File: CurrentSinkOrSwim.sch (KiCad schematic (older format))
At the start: 0 parts

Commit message: Adding preliminary components (without values) to the schematic.
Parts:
- added C? (x2): C, symbol C
- added P?: CONN_01X02, symbol CONN_01X02
- added Q?: MOSFET_N, symbol MOSFET_N
- added R? (x2): R, symbol R
- added RV?: POT, symbol POT
- added U? (x2): LMV358, symbol LMV358
- added U?: TC1016, symbol TC1016
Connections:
- net labels added: GND
- wire segments 0 -> 36

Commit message: Updating The Schematic With Part Numbers
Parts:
- removed U?: TC1016, symbol TC1016
- added C?: C, symbol C
- added R?: 0, symbol R
- added U?: TC1016, symbol TC1016
- Q?: value MOSFET_N -> BUK9575; MPN (none) -> BUK9575-100A,127
- R?: value R -> .1; MPN (none) -> AC01000001007JA100
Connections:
- net labels added: 2.7V
- wire segments 36 -> 34
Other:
- moved on the sheet: C?, P?
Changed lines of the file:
@@
 P 6950 4550
 F 0 "R?" V 7030 4550 50  0000 C CNN
-F 1 "R" V 6957 4551 50  0000 C CNN
+F 1 ".1" V 6957 4551 50  0000 C CNN
 F 2 "" V 6880 4550 30  0000 C CNN
 F 3 "" H 6950 4550 30  0000 C CNN
+F 4 "AC01000001007JA100" V 6950 4550 60  0001 C CNN "MPN"
 	1    6950 4550
 	1    0    0    -1
@@
 P 6850 3100
 F 0 "Q?" H 6860 3270 50  0000 R CNN
-F 1 "MOSFET_N" H 6800 2950 50  0000 R CNN
+F 1 "BUK9575" H 6800 2950 50  0000 R CNN
 F 2 "" H 6850 3100 60  0000 C CNN
 F 3 "" H 6850 3100 60  0000 C CNN
+F 4 "BUK9575-100A,127" H 6850 3100 60  0001 C CNN "MPN"
 	1    6850 3100
 	1    0    0    -1
@@
 $EndComp
 Wire Wire Line
-	6950 4800 6950 4850
-Wire Wire Line
-	6950 4850 6950 5000
-Wire Wire Line
-	6950 3300 6950 4000
-Wire Wire Line
-	6950 4000 6950 4300
+	6950 4800 6950 5000
+Wire Wire Line
+	6950 3300 6950 4300
 Wire Wire Line
 	6650 3100 6000 3100
@@
 Connection ~ 6950 4000
 Wire Wire Line
-	5400 1950 5400 2700
-Wire Wire Line
 	5000 3000 4150 3000
 Wire Wire Line
@@
 	4150 3950 3600 3950
 Wire Wire Line
-	3600 3850 3600 3950
-Wire Wire Line
-	3600 3950 3600 4050
+	3600 3850 3600 4050
 Connection ~ 3600 3950
 Wire Wire Line
@@
 Connection ~ 6950 4850
 Wire Wire Line
-	6500 1950 6600 1950
-Wire Wire Line
-	6600 1950 6950 1950
-Wire Wire Line
-	6950 1950 8100 1950
-Wire Wire Line
-	6950 1950 6950 2900
-$Comp
-L TC1016 U?
-U 1 1 54CE8C07
-P 6100 2000
-F 0 "U?" H 6250 1804 60  0000 C CNN
-F 1 "TC1016" H 6100 2200 60  0000 C CNN
-F 2 "" H 6100 2000 60  0000 C CNN
-F 3 "" H 6100 2000 60  0000 C CNN
-	1    6100 2000
-	-1   0    0    -1
-$EndComp
-Connection ~ 6950 1950
-Connection ~ 5400 1950
+	6200 1250 8100 1250
+Wire Wire Line
+	6950 1250 6950 2900
+Connection ~ 6950 1250
 $Comp
 L GND #PWR?
 U 1 1 54CE8D06
-P 6100 2500
-F 0 "#PWR?" H 6100 2250 60  0001 C CNN
-F 1 "GND" H 6100 2350 60  0000 C CNN
-F 2 "" H 6100 2500 60  0000 C CNN
-F 3 "" H 6100 2500 60  0000 C CNN
-	1    6100 2500
-	1    0    0    -1
-$EndComp
-Wire Wire Line
-	6100 2500 6100 2450
-Wire Wire Line
-	6100 2450 6100 2350
-Wire Wire Line
-	6100 2350 6100 2250
+P 5800 2150
+F 0 "#PWR?" H 5800 1900 60  0001 C CNN
+F 1 "GND" H 5800 2000 60  0000 C CNN
+F 2 "" H 5800 2150 60  0000 C CNN
+F 3 "" H 5800 2150 60  0000 C CNN
+	1    5800 2150
+	1    0    0    -1
+$EndComp
 $Comp
 L C C?
 U 1 1 54CE8F07
-P 6600 2250
-F 0 "C?" H 6650 2350 50  0000 L CNN
-F 1 "C" H 6650 2150 50  0000 L CNN
-F 2 "" H 6638 2100 30  0000 C CNN
-F 3 "" H 6600 2250 60  0000 C CNN
-	1    6600 2250
+P 6600 1550
+F 0 "C?" H 6650 1650 50  0000 L CNN
+F 1 "C" H 6650 1450 50  0000 L CNN
+F 2 "" H 6638 1400 30  0000 C CNN
+F 3 "" H 6600 1550 60  0000 C CNN
+	1    6600 1550
 	1    0    0    -1
 $EndComp
@@
 L C C?
 U 1 1 54CE8F9A
-P 5600 2250
-F 0 "C?" H 5650 2350 50  0000 L CNN
-F 1 "C" H 5650 2150 50  0000 L CNN
-F 2 "" H 5638 2100 30  0000 C CNN
-F 3 "" H 5600 2250 60  0000 C CNN
-	1    5600 2250
-	1    0    0    -1
-$EndComp
-Wire Wire Line
-	5600 1950 5600 2050
-Connection ~ 5600 1950
-Wire Wire Line
-	5600 2450 6100 2450
-Connection ~ 6100 2450
-Wire Wire Line
-	6600 2450 6250 2450
-Wire Wire Line
-	6250 2450 6250 2350
-Wire Wire Line
-	6250 2350 6100 2350
-Connection ~ 6100 2350
-Wire Wire Line
-	6600 2050 6600 1950
-Connection ~ 6600 1950
+P 5000 1600
+F 0 "C?" H 5050 1700 50  0000 L CNN
+F 1 "C" H 5050 1500 50  0000 L CNN
+F 2 "" H 5038 1450 30  0000 C CNN
+F 3 "" H 5000 1600 60  0000 C CNN
+	1    5000 1600
+	1    0    0    -1
+$EndComp
+Wire Wire Line
+	6600 1350 6600 1250
+Connection ~ 6600 1250
 $Comp
 L POT RV?
@@
 $EndComp
 Wire Wire Line
-	3750 3600 3750 1950
-Wire Wire Line
-	3750 1950 5400 1950
-Wire Wire Line
-	5400 1950 5600 1950
-Wire Wire Line
-	5600 1950 5700 1950
+	3750 1250 3750 3600
 $Comp
 L CONN_01X02 P?
 U 1 1 54CEA02B
-P 8300 2000
-F 0 "P?" H 8300 2150 50  0000 C CNN
-F 1 "CONN_01X02" V 8400 2000 50  0000 C CNN
-F 2 "" H 8300 2000 60  0000 C CNN
-F 3 "" H 8300 2000 60  0000 C CNN
-	1    8300 2000
-	1    0    0    -1
-$EndComp
-Wire Wire Line
-	8100 2050 7900 2050
-Wire Wire Line
-	7900 2050 7900 2350
+P 8300 1300
+F 0 "P?" H 8300 1450 50  0000 C CNN
+F 1 "CONN_01X02" V 8400 1300 50  0000 C CNN
+F 2 "" H 8300 1300 60  0000 C CNN
+F 3 "" H 8300 1300 60  0000 C CNN
+	1    8300 1300
+	1    0    0    -1
+$EndComp
+Wire Wire Line
+	8100 1350 7900 1350
+Wire Wire Line
+	7900 1350 7900 2350
 $Comp
 L GND #PWR?
@@
 	1    0    0    -1
 $EndComp
+$Comp
+L TC1016 U?
+U 1 1 54D813FD
+P 5800 1450
+F 0 "U?" H 5950 1254 60  0000 C CNN
+F 1 "TC1016" H 5800 1850 60  0000 C CNN
+F 2 "" H 5800 1450 60  0000 C CNN
+F 3 "" H 5800 1450 60  0000 C CNN
+	1    5800 1450
+	-1   0    0    -1
+$EndComp
+Wire Wire Line
+	6600 1750 6600 2050
+Wire Wire Line
+	3750 1250 5400 1250
+Wire Wire Line
+	5000 1250 5000 1400
+Wire Wire Line
+	5000 1800 5000 1900
+Wire Wire Line
+	5000 1900 5800 1900
+Connection ~ 6400 1250
+$Comp
+L R R?
+U 1 1 54D81C67
+P 6400 1550
+F 0 "R?" V 6480 1550 40  0000 C CNN
+F 1 "0" V 6407 1551 40  0000 C CNN
+F 2 "" V 6330 1550 30  0000 C CNN
+F 3 "" H 6400 1550 30  0000 C CNN
+F 4 "Value" H 6400 1550 60  0001 C CNN "MPN"
+	1    6400 1550
+	1    0    0    -1
+$EndComp
+Wire Wire Line
+	5800 1700 5800 2150
+Wire Wire Line
+	6600 2050 5800 2050
+Connection ~ 5800 2050
+Wire Wire Line
+	6400 1300 6400 1250
+Wire Wire Line
+	6400 1800 6400 1900
+Wire Wire Line
+	6400 1900 6200 1900
+Wire Wire Line
+	6200 1900 6200 1400
+Connection ~ 5000 1250
+Wire Wire Line
+	3750 2250 5400 2250
+Wire Wire Line
+	5400 2250 5400 2700
+Connection ~ 3750 2250
+$Comp
+L GND #PWR?
+U 1 1 54D82007
+P 4800 2800
+F 0 "#PWR?" H 4800 2550 60  0001 C CNN
+F 1 "GND" H 4800 2650 60  0000 C CNN
+F 2 "" H 4800 2800 60  0000 C CNN
+F 3 "" H 4800 2800 60  0000 C CNN
+	1    4800 2800
+	1    0    0    -1
+$EndComp
+$Comp
+L C C?
+U 1 1 54D8201D
+P 4800 2550
+F 0 "C?" H 4850 2650 50  0000 L CNN
+F 1 "C" H 4850 2450 50  0000 L CNN
+F 2 "" H 4838 2400 30  0000 C CNN
+F 3 "" H 4800 2550 60  0000 C CNN
+	1    4800 2550
+	1    0    0    -1
+$EndComp
+Wire Wire Line
+	4800 2350 4800 2250
+Connection ~ 4800 2250
+Wire Wire Line
+	4800 2800 4800 2750
+Text Label 4400 2250 0    60   ~ 0
+2.7V
 $EndSCHEMATC

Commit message: Finding A Higher Rated Linear Regulator
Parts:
- removed U?: TC1016, symbol TC1016
- added P?: CONN_01X03, symbol CONN_01X03
- added P?: CONN_01X02, symbol CONN_01X02
- added R?: 27K, symbol R
- added R?: 21.6K, symbol R
- added U?: LM2931D-R, symbol LM2931D-R
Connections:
- wire segments 34 -> 52
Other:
- note added: "Battery Pack"
- note added: "Current Sink Input"
- moved on the sheet: C?, R?
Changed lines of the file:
@@
 	3600 4850 6950 4850
 Connection ~ 6950 4850
-Wire Wire Line
-	6200 1250 8100 1250
-Wire Wire Line
-	6950 1250 6950 2900
-Connection ~ 6950 1250
 $Comp
 L GND #PWR?
@@
 L C C?
 U 1 1 54CE8F9A
-P 5000 1600
-F 0 "C?" H 5050 1700 50  0000 L CNN
-F 1 "C" H 5050 1500 50  0000 L CNN
-F 2 "" H 5038 1450 30  0000 C CNN
-F 3 "" H 5000 1600 60  0000 C CNN
-	1    5000 1600
-	1    0    0    -1
-$EndComp
-Wire Wire Line
-	6600 1350 6600 1250
-Connection ~ 6600 1250
+P 4400 1700
+F 0 "C?" H 4450 1800 50  0000 L CNN
+F 1 "C" H 4450 1600 50  0000 L CNN
+F 2 "" H 4438 1550 30  0000 C CNN
+F 3 "" H 4400 1700 60  0000 C CNN
+	1    4400 1700
+	1    0    0    -1
+$EndComp
 $Comp
 L POT RV?
@@
 $EndComp
 Wire Wire Line
-	3750 1250 3750 3600
+	3750 900  3750 3600
 $Comp
 L CONN_01X02 P?
@@
 	1    0    0    -1
 $EndComp
-$Comp
-L TC1016 U?
-U 1 1 54D813FD
-P 5800 1450
-F 0 "U?" H 5950 1254 60  0000 C CNN
-F 1 "TC1016" H 5800 1850 60  0000 C CNN
-F 2 "" H 5800 1450 60  0000 C CNN
-F 3 "" H 5800 1450 60  0000 C CNN
-	1    5800 1450
-	-1   0    0    -1
-$EndComp
-Wire Wire Line
-	6600 1750 6600 2050
-Wire Wire Line
-	3750 1250 5400 1250
-Wire Wire Line
-	5000 1250 5000 1400
-Wire Wire Line
-	5000 1800 5000 1900
-Wire Wire Line
-	5000 1900 5800 1900
-Connection ~ 6400 1250
+Wire Wire Line
+	6600 2050 6600 1750
 $Comp
 L R R?
 U 1 1 54D81C67
-P 6400 1550
-F 0 "R?" V 6480 1550 40  0000 C CNN
-F 1 "0" V 6407 1551 40  0000 C CNN
-F 2 "" V 6330 1550 30  0000 C CNN
-F 3 "" H 6400 1550 30  0000 C CNN
-F 4 "Value" H 6400 1550 60  0001 C CNN "MPN"
-	1    6400 1550
+P 6400 1450
+F 0 "R?" V 6480 1450 40  0000 C CNN
+F 1 "0" V 6407 1451 40  0000 C CNN
+F 2 "" V 6330 1450 30  0000 C CNN
+F 3 "" H 6400 1450 30  0000 C CNN
+F 4 "Value" H 6400 1450 60  0001 C CNN "MPN"
+	1    6400 1450
 	1    0    0    -1
 $EndComp
@@
 	5800 1700 5800 2150
 Wire Wire Line
-	6600 2050 5800 2050
+	5700 2050 6600 2050
 Connection ~ 5800 2050
 Wire Wire Line
-	6400 1300 6400 1250
-Wire Wire Line
-	6400 1800 6400 1900
-Wire Wire Line
-	6400 1900 6200 1900
-Wire Wire Line
-	6200 1900 6200 1400
-Connection ~ 5000 1250
+	6400 1100 6400 1300
 Wire Wire Line
 	3750 2250 5400 2250
@@
 Text Label 4400 2250 0    60   ~ 0
 2.7V
+$Comp
+L LM2931D-R U?
+U 1 1 54D82F07
+P 5850 1400
+F 0 "U?" H 6100 1250 60  0000 C CNN
+F 1 "LM2931D-R" H 5850 2050 60  0000 C CNN
+F 2 "" H 5700 1400 60  0000 C CNN
+F 3 "" H 5700 1400 60  0000 C CNN
+	1    5850 1400
+	-1   0    0    -1
+$EndComp
+Wire Wire Line
+	3750 900  5400 900
+Wire Wire Line
+	4400 900  4400 1500
+Connection ~ 4400 900
+$Comp
+L R R?
+U 1 1 54D8307E
+P 4950 1150
+F 0 "R?" V 5030 1150 40  0000 C CNN
+F 1 "27K" V 4957 1151 40  0000 C CNN
+F 2 "" V 4880 1150 30  0000 C CNN
+F 3 "" H 4950 1150 30  0000 C CNN
+F 4 "Value" H 4950 1150 60  0001 C CNN "MPN"
+	1    4950 1150
+	1    0    0    -1
+$EndComp
+$Comp
+L R R?
+U 1 1 54D83280
+P 4950 1800
+F 0 "R?" V 5030 1800 40  0000 C CNN
+F 1 "21.6K" V 4957 1801 40  0000 C CNN
+F 2 "" V 4880 1800 30  0000 C CNN
+F 3 "" H 4950 1800 30  0000 C CNN
+	1    4950 1800
+	1    0    0    -1
+$EndComp
+Wire Wire Line
+	4400 2100 5800 2100
+Wire Wire Line
+	4950 2100 4950 2050
+Connection ~ 5800 2100
+Wire Wire Line
+	4400 2100 4400 1900
+Connection ~ 4950 2100
+Wire Wire Line
+	4950 1400 4950 1550
+Wire Wire Line
+	5400 1100 5200 1100
+Wire Wire Line
+	5200 1100 5200 1500
+Wire Wire Line
+	5200 1500 4950 1500
+Connection ~ 4950 1500
+Wire Wire Line
+	6300 1100 6400 1100
+Wire Wire Line
+	6600 1350 6600 900
+Wire Wire Line
+	7900 900  7900 1250
+Wire Wire Line
+	7900 1250 8100 1250
+Connection ~ 6600 900
+Wire Wire Line
+	6400 1700 6400 2050
+Connection ~ 6400 2050
+Wire Wire Line
+	5900 1700 5900 2050
+Connection ~ 5900 2050
+Wire Wire Line
+	6000 1700 6000 2050
+Connection ~ 6000 2050
+Wire Wire Line
+	5700 2050 5700 1700
+Wire Wire Line
+	7900 900  6950 900
+Wire Wire Line
+	6950 800  6950 2900
+$Comp
+L CONN_01X03 P?
+U 1 1 54D855F7
+P 6850 600
+F 0 "P?" H 6850 800 50  0000 C CNN
+F 1 "CONN_01X03" V 6950 600 50  0000 C CNN
+F 2 "" H 6850 600 60  0000 C CNN
+F 3 "" H 6850 600 60  0000 C CNN
+	1    6850 600
+	0    -1   -1   0
+$EndComp
+Connection ~ 6950 900
+Wire Wire Line
+	6850 800  6850 900
+Wire Wire Line
+	6850 900  6300 900
+Wire Wire Line
+	6750 800  6350 800
+Wire Wire Line
+	6350 800  6350 650
+Wire Wire Line
+	6350 650  2800 650
+Wire Wire Line
+	2800 650  2800 1250
+$Comp
+L CONN_01X02 P?
+U 1 1 54D858EB
+P 2750 1450
+F 0 "P?" H 2750 1600 50  0000 C CNN
+F 1 "CONN_01X02" V 2850 1450 50  0000 C CNN
+F 2 "" H 2750 1450 60  0000 C CNN
+F 3 "" H 2750 1450 60  0000 C CNN
+	1    2750 1450
+	0    1    1    0
+$EndComp
+$Comp
+L GND #PWR?
+U 1 1 54D85A15
+P 2000 1600
+F 0 "#PWR?" H 2000 1350 60  0001 C CNN
+F 1 "GND" H 2000 1450 60  0000 C CNN
+F 2 "" H 2000 1600 60  0000 C CNN
+F 3 "" H 2000 1600 60  0000 C CNN
+	1    2000 1600
+	1    0    0    -1
+$EndComp
+Wire Wire Line
+	2000 1600 2000 1100
+Wire Wire Line
+	2000 1100 2700 1100
+Wire Wire Line
+	2700 1100 2700 1250
+Text Notes 2500 1750 0    60   ~ 0
+Battery Pack
+Text Notes 8600 1350 0    60   ~ 0
+Current Sink Input
 $EndSCHEMATC

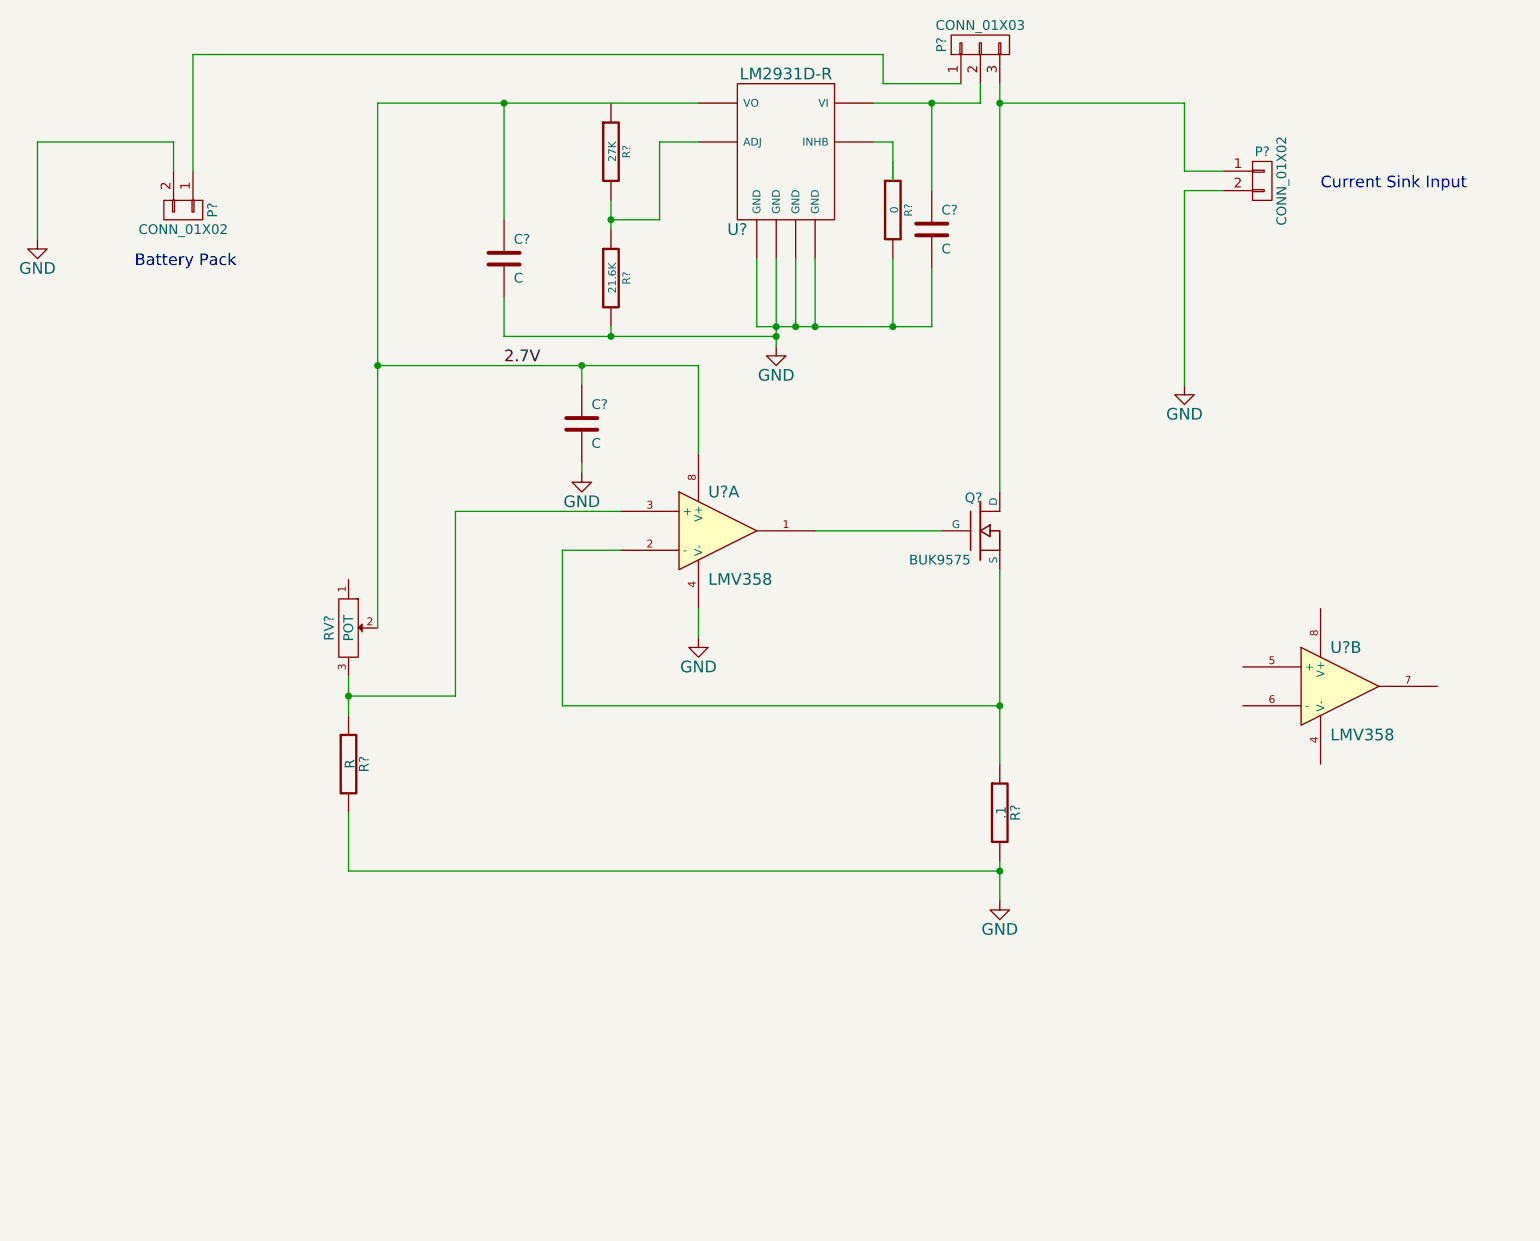
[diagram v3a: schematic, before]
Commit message: Breaking the schematic into hierarchical sheets and updating VoltageControl circuit
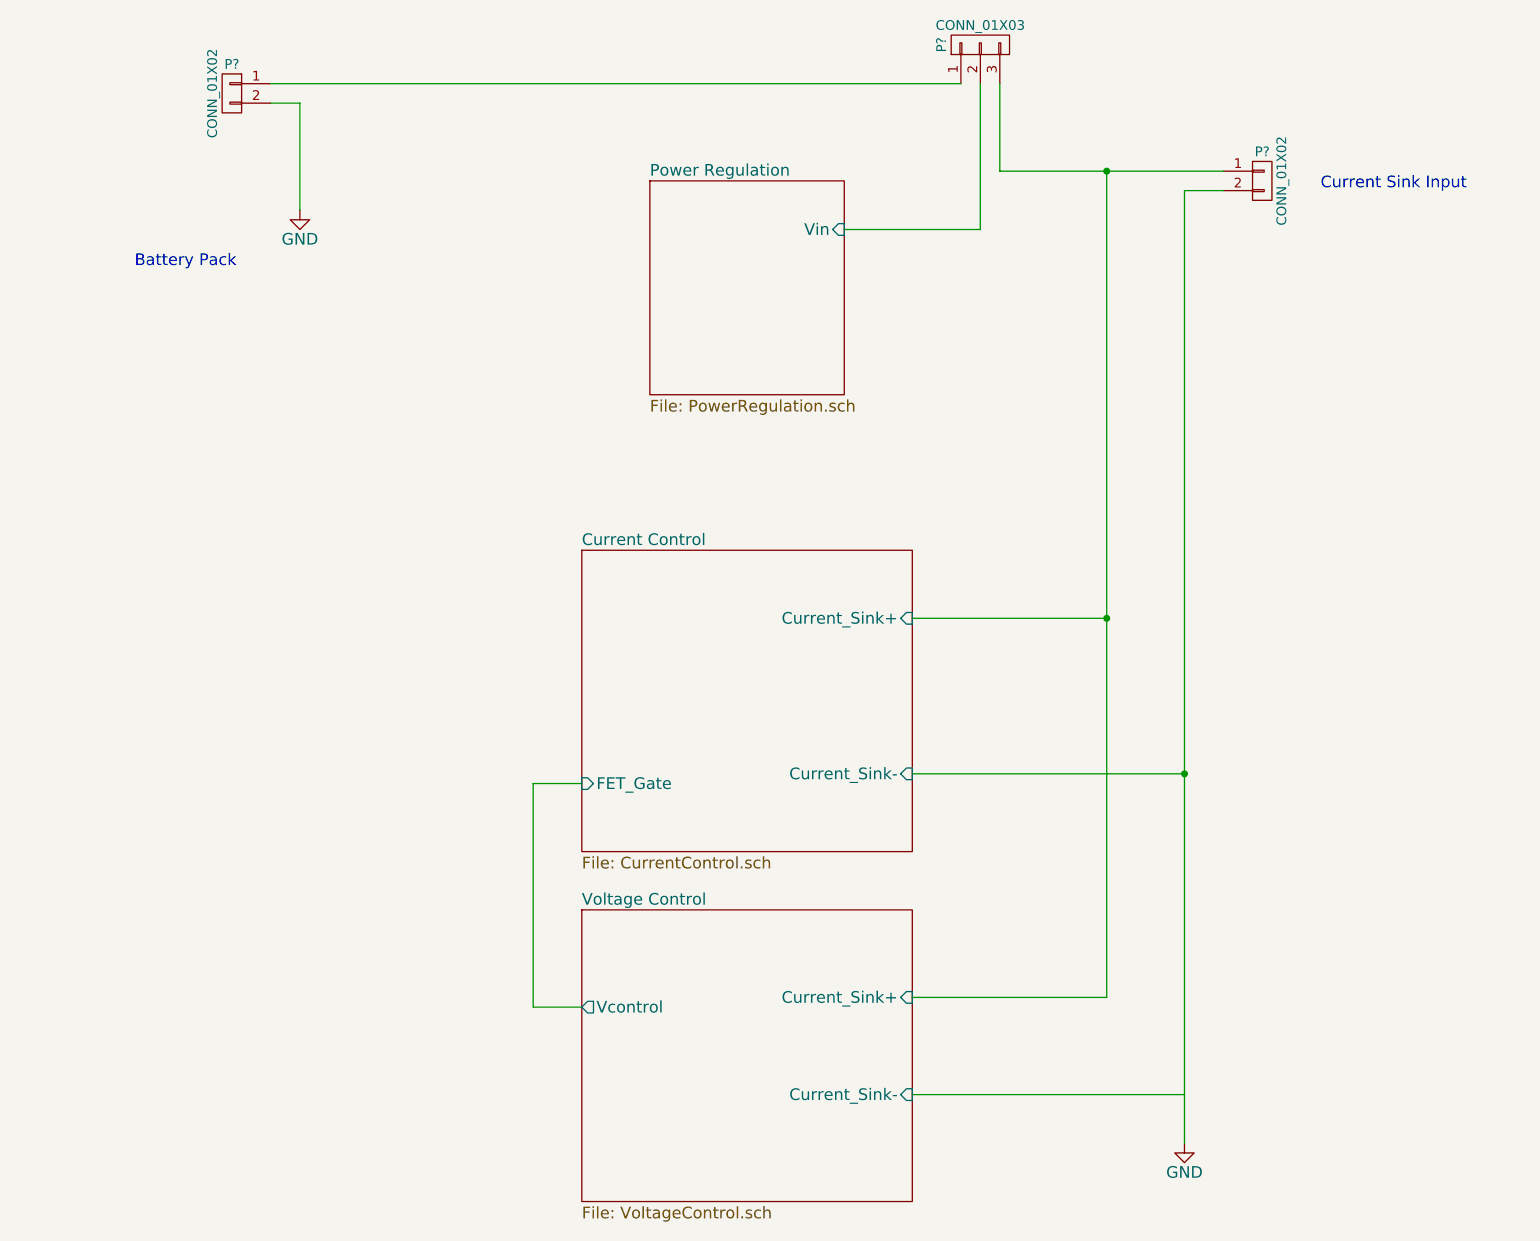
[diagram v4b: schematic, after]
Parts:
- removed C? (x3): C, symbol C
- removed Q?: BUK9575, symbol MOSFET_N
- removed R?: .1, symbol R
- removed R?: R, symbol R
- removed R?: 0, symbol R
- removed R?: 27K, symbol R
- removed R?: 21.6K, symbol R
- removed RV?: POT, symbol POT
- removed U? (x2): LMV358, symbol LMV358
- removed U?: LM2931D-R, symbol LM2931D-R
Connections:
- net labels removed: 2.7V
- wire segments 52 -> 22
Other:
- moved on the sheet: P?

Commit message: Initial Annotation
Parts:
- gave numbers to parts that had none: 3
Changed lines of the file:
@@
 $EndDescr
 $Comp
-L CONN_01X02 P?
+L CONN_01X02 P103
 U 1 1 54CEA02B
 P 8300 1300
-F 0 "P?" H 8300 1450 50  0000 C CNN
+F 0 "P103" H 8300 1450 50  0000 C CNN
 F 1 "CONN_01X02" V 8400 1300 50  0000 C CNN
 F 2 "" H 8300 1300 60  0000 C CNN
@@
 $EndComp
 $Comp
-L CONN_01X03 P?
+L CONN_01X03 P102
 U 1 1 54D855F7
 P 6850 600
-F 0 "P?" H 6850 800 50  0000 C CNN
+F 0 "P102" H 6850 800 50  0000 C CNN
 F 1 "CONN_01X03" V 6950 600 50  0000 C CNN
 F 2 "" H 6850 600 60  0000 C CNN
@@
 $EndComp
 $Comp
-L CONN_01X02 P?
+L CONN_01X02 P101
 U 1 1 54D858EB
 P 3000 850
-F 0 "P?" H 3000 1000 50  0000 C CNN
+F 0 "P101" H 3000 1000 50  0000 C CNN
 F 1 "CONN_01X02" V 3100 850 50  0000 C CNN
 F 2 "" H 3000 850 60  0000 C CNN
@@
 $EndComp
 $Comp
-L GND #PWR?
+L GND #PWR101
 U 1 1 54D85A15
 P 3350 1450
-F 0 "#PWR?" H 3350 1200 60  0001 C CNN
+F 0 "#PWR101" H 3350 1200 60  0001 C CNN
 F 1 "GND" H 3350 1300 60  0000 C CNN
 F 2 "" H 3350 1450 60  0000 C CNN
@@
 	4550 4400 4800 4400
 $Comp
-L GND #PWR?
+L GND #PWR102
 U 1 1 54DB4AD2
 P 7900 6250
-F 0 "#PWR?" H 7900 6000 60  0001 C CNN
+F 0 "#PWR102" H 7900 6000 60  0001 C CNN
 F 1 "GND" H 7900 6100 60  0000 C CNN
 F 2 "" H 7900 6250 60  0000 C CNN
